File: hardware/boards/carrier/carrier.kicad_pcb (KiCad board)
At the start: 4 copper layers, 106 x 34.3 mm, 50 parts, among them J1 XT30PW(2+2), Q1 IPB020N10N5LF, Q2 2N7002, Q3 2N7002, U1 STM32G031G6U6, U2 LM5163DDAR, U3 LMX5069MS, U4 INA237AIDGSR

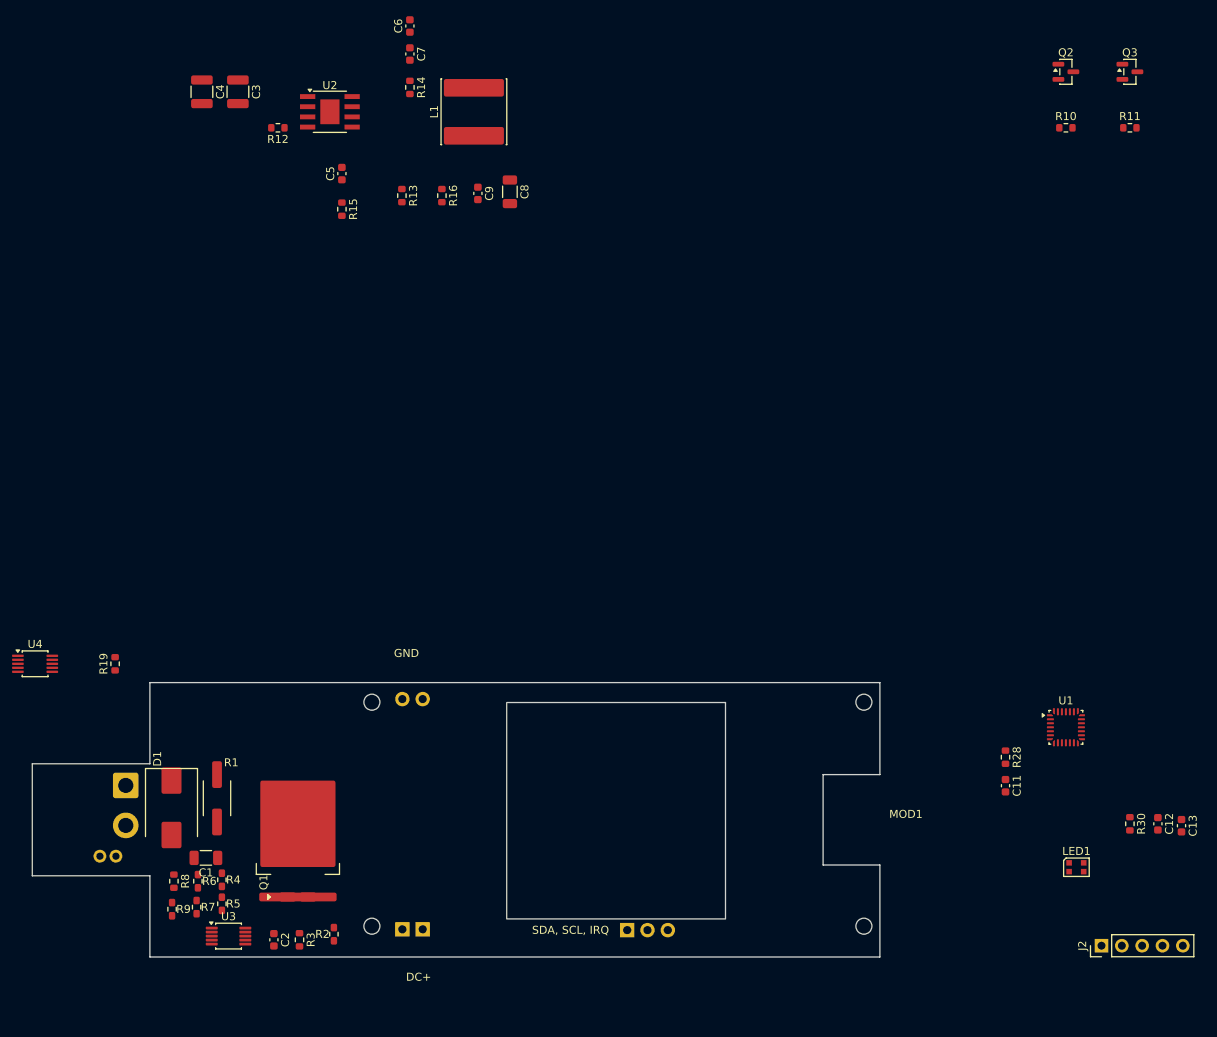
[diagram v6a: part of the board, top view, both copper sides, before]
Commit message: layout: place carrier power-control components
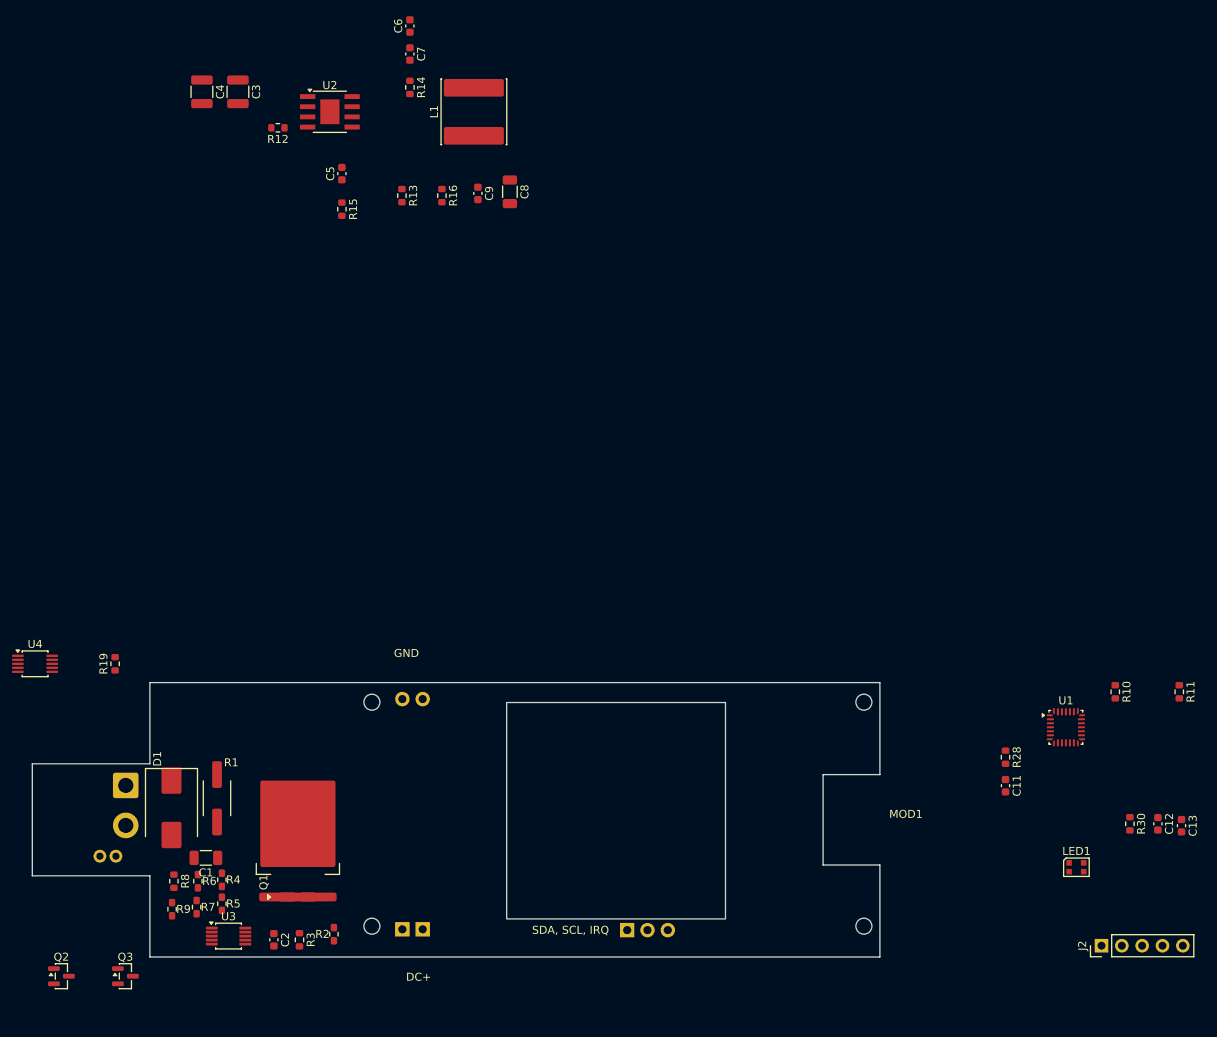
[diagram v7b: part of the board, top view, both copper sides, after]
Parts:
- moved Q2 169.0 mm to (104.4, 133.1)
- moved Q3 169.0 mm to (112.4, 133.1)
- moved R10 70.8 mm to (236.2, 97.5), turned to -90 degrees
- moved R11 70.8 mm to (244.2, 97.5), turned to -90 degrees
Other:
- board text removed: "PD ENABLE CONTROL Q2-Q3, R10-R11 - MOD1 on board"
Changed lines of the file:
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@@
 	(footprint "Resistor_SMD:R_0603_1608Metric"
 		(layer "F.Cu")
-		(at 238 27)
+		(at 244.175 97.5 -90)
 		(descr "Resistor SMD 0603 (1608 Metric), square (rectangular) end terminal, IPC-7351 nominal, (Body size source: IPC-SM-782 page 72, https://www.pcb-3d.com/wordpress/wp-content/uploads/ipc-sm-782a_amendment_1_and_2.pdf)")
 		(tags "resistor")
 		(property "Reference" "R11"
-			(at 0 -1.43 0)
+			(at 0 -1.43 90)
 			(layer "F.SilkS")
 			(effects
@@
 		)
 		(property "Value" "10k"
-			(at 0 1.43 0)
+			(at 0 1.43 90)
 			(layer "F.Fab")
 			(effects
@@
 		)
 		(property "Datasheet" ""
-			(at 0 0 0)
+			(at 0 0 90)
 			(layer "F.Fab")
 			(hide yes)
@@
 		)
 		(property "Description" "Resistor"
-			(at 0 0 0)
+			(at 0 0 90)
 			(layer "F.Fab")
 			(hide yes)
@@
 		)
 		(property "KiLib_Generator" "SMD_2terminal_chip_molded"
-			(at 0 0 0)
+			(at 0 0 90)
 			(layer "F.SilkS")
 			(hide yes)
@@
 		(duplicate_pad_numbers_are_jumpers no)
 		(fp_line
-			(start -0.237258 -0.5225)
-			(end 0.237258 -0.5225)
+			(start -0.237258 0.5225)
+			(end 0.237258 0.5225)
 			(stroke
 				(width 0.12)
@@
 		)
 		(fp_line
-			(start -0.237258 0.5225)
-			(end 0.237258 0.5225)
+			(start -0.237258 -0.5225)
+			(end 0.237258 -0.5225)
 			(stroke
 				(width 0.12)
@@
 		)
 		(fp_text user "${REFERENCE}"
-			(at 0 0 0)
+			(at 0 0 90)
 			(layer "F.Fab")
 			(effects
@@
 		)
 		(pad "1" smd roundrect
-			(at -0.825 0)
+			(at -0.825 0 270)
 			(size 0.8 0.95)
 			(layers "F.Cu" "F.Mask" "F.Paste")
@@
 		)
 		(pad "2" smd roundrect
-			(at 0.825 0)
+			(at 0.825 0 270)
 			(size 0.8 0.95)
 			(layers "F.Cu" "F.Mask" "F.Paste")
@@
 	(footprint "Package_TO_SOT_SMD:SOT-23"
 		(layer "F.Cu")
-		(at 230 20)
+		(at 104.4375 133.05)
 		(descr "SOT, 3 Pin (JEDEC TO-236 Var AB https://www.jedec.org/document_search?search_api_views_fulltext=TO-236)")
 		(tags "SOT TO_SOT_SMD")
@@
 	(footprint "Package_TO_SOT_SMD:SOT-23"
 		(layer "F.Cu")
-		(at 238 20)
+		(at 112.4375 133.05)
 		(descr "SOT, 3 Pin (JEDEC TO-236 Var AB https://www.jedec.org/document_search?search_api_views_fulltext=TO-236)")
 		(tags "SOT TO_SOT_SMD")
@@
 	(footprint "Resistor_SMD:R_0603_1608Metric"
 		(layer "F.Cu")
-		(at 230 27)
+		(at 236.175 97.5 -90)
 		(descr "Resistor SMD 0603 (1608 Metric), square (rectangular) end terminal, IPC-7351 nominal, (Body size source: IPC-SM-782 page 72, https://www.pcb-3d.com/wordpress/wp-content/uploads/ipc-sm-782a_amendment_1_and_2.pdf)")
 		(tags "resistor")
 		(property "Reference" "R10"
-			(at 0 -1.43 0)
+			(at 0 -1.43 90)
 			(layer "F.SilkS")
 			(effects
@@
 		)
 		(property "Value" "100k"
-			(at 0 1.43 0)
+			(at 0 1.43 90)
 			(layer "F.Fab")
 			(effects
@@
 		)
 		(property "Datasheet" ""
-			(at 0 0 0)
+			(at 0 0 90)
 			(layer "F.Fab")
 			(hide yes)
@@
 		)
 		(property "Description" "Resistor"
-			(at 0 0 0)
+			(at 0 0 90)
 			(layer "F.Fab")
 			(hide yes)
@@
 		)
 		(property "KiLib_Generator" "SMD_2terminal_chip_molded"
-			(at 0 0 0)
+			(at 0 0 90)
 			(layer "F.SilkS")
 			(hide yes)
@@
 		(duplicate_pad_numbers_are_jumpers no)
 		(fp_line
-			(start -0.237258 -0.5225)
-			(end 0.237258 -0.5225)
+			(start -0.237258 0.5225)
+			(end 0.237258 0.5225)
 			(stroke
 				(width 0.12)
@@
 		)
 		(fp_line
-			(start -0.237258 0.5225)
-			(end 0.237258 0.5225)
+			(start -0.237258 -0.5225)
+			(end 0.237258 -0.5225)
 			(stroke
 				(width 0.12)
@@
 		)
 		(fp_text user "${REFERENCE}"
-			(at 0 0 0)
+			(at 0 0 90)
 			(layer "F.Fab")
 			(effects
@@
 		)
 		(pad "1" smd roundrect
-			(at -0.825 0)
+			(at -0.825 0 270)
 			(size 0.8 0.95)
 			(layers "F.Cu" "F.Mask" "F.Paste")
@@
 		)
 		(pad "2" smd roundrect
-			(at 0.825 0)
+			(at 0.825 0 270)
 			(size 0.8 0.95)
 			(layers "F.Cu" "F.Mask" "F.Paste")
@@
 	)
 	(gr_rect
-		(start 225 15)
-		(end 242 31)
-		(stroke
-			(width 0.25)
-			(type default)
-		)
-		(fill no)
-		(layer "Cmts.User")
-	)
-	(gr_rect
 		(start 231 171)
 		(end 246 179)
@@
 		(layer "Cmts.User")
 		(effects
-			(font
-				(size 1.2 1.2)
-				(thickness 0.2)
-				(bold yes)
-			)
-			(justify left bottom)
-		)
-	)
-	(gr_text "PD ENABLE CONTROL\nQ2-Q3, R10-R11 - MOD1 on board"
-		(at 225 13 0)
-		(layer "Cmts.User")
-		(effects
